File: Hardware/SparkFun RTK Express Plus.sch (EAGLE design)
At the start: 111 parts, among them J13 Internal, J16 MICRO-SD-PUSH-PUSH-EXT-PIN, J17 Qwiic Right Angle, J3 USB Female Type C Connector, J4 External, J5 USB Female Type C Connector, Q1 SIL2308-TP, Q2 MBT3904DW1T1, U1 74HC4052D, U10 MCP73833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

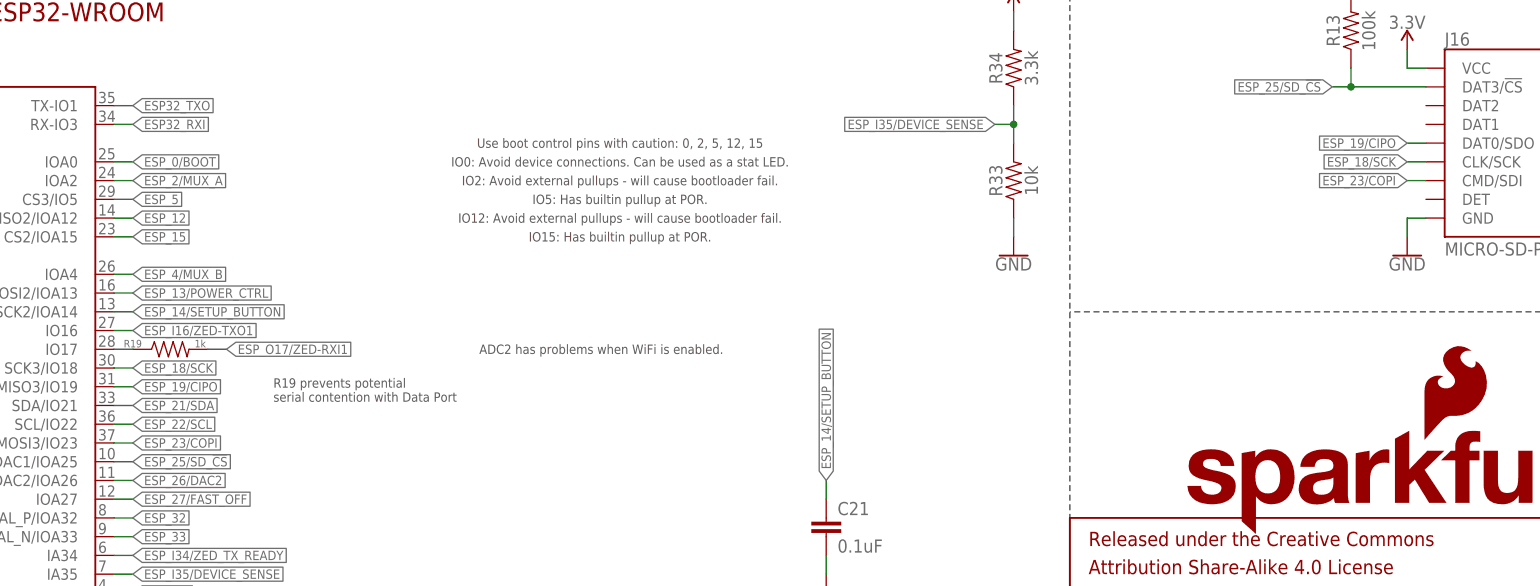
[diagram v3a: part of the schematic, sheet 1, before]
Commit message: v13 - Change to LIF overlay connector. Change ESP32 FP. Pull ground from accel.
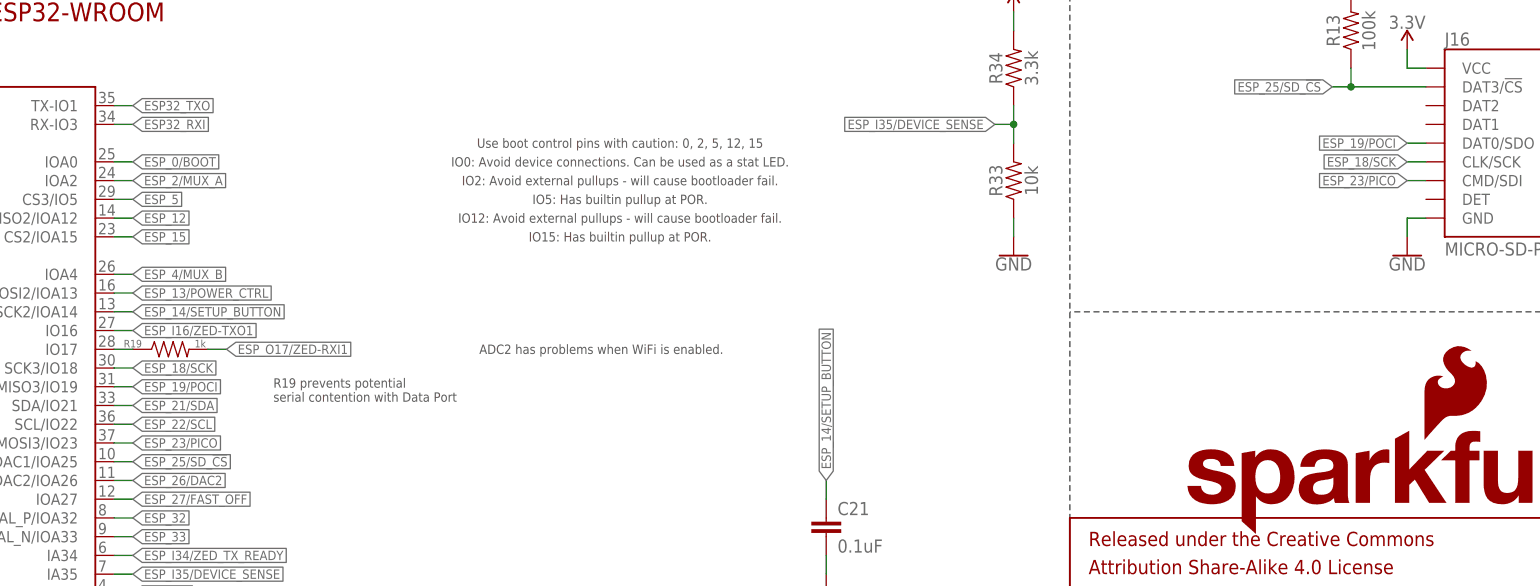
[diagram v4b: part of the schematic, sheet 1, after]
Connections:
- net ESP_19/CIPO renamed ESP_19/POCI
- net ESP_23/COPI renamed ESP_23/PICO
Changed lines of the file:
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@@
 <grid distance="0.1" unitdist="inch" unit="inch" style="lines" multiple="1" display="no" altdistance="0.01" altunitdist="inch" altunit="inch"/>
 <layers>
-<layer number="1" name="Top" color="4" fill="1" visible="yes" active="no"/>
-<layer number="2" name="Route2" color="1" fill="3" visible="yes" active="no"/>
-<layer number="3" name="Route3" color="4" fill="3" visible="yes" active="no"/>
-<layer number="4" name="Route4" color="1" fill="4" visible="yes" active="no"/>
-<layer number="5" name="Route5" color="4" fill="4" visible="yes" active="no"/>
-<layer number="6" name="Route6" color="1" fill="8" visible="yes" active="no"/>
-<layer number="7" name="Route7" color="4" fill="8" visible="yes" active="no"/>
-<layer number="8" name="Route8" color="1" fill="2" visible="yes" active="no"/>
-<layer number="9" name="Route9" color="4" fill="2" visible="yes" active="no"/>
-<layer number="10" name="Route10" color="1" fill="7" visible="yes" active="no"/>
-<layer number="11" name="Route11" color="4" fill="7" visible="yes" active="no"/>
-<layer number="12" name="Route12" color="1" fill="5" visible="yes" active="no"/>
-<layer number="13" name="Route13" color="4" fill="5" visible="yes" active="no"/>
-<layer number="14" name="Route14" color="1" fill="6" visible="yes" active="no"/>
-<layer number="15" name="Route15" color="4" fill="6" visible="yes" active="no"/>
-<layer number="16" name="Bottom" color="1" fill="1" visible="yes" active="no"/>
-<layer number="17" name="Pads" color="2" fill="1" visible="yes" active="no"/>
-<layer number="18" name="Vias" color="2" fill="1" visible="yes" active="no"/>
-<layer number="19" name="Unrouted" color="6" fill="1" visible="yes" active="no"/>
-<layer number="20" name="Dimension" color="24" fill="1" visible="yes" active="no"/>
-<layer number="21" name="tPlace" color="16" fill="1" visible="yes" active="no"/>
-<layer number="22" name="bPlace" color="14" fill="1" visible="yes" active="no"/>
-<layer number="23" name="tOrigins" color="15" fill="1" visible="yes" active="no"/>
-<layer number="24" name="bOrigins" color="15" fill="1" visible="yes" active="no"/>
-<layer number="25" name="tNames" color="7" fill="1" visible="yes" active="no"/>
-<layer number="26" name="bNames" color="7" fill="1" visible="yes" active="no"/>
-<layer number="27" name="tValues" color="7" fill="1" visible="yes" active="no"/>
-<layer number="28" name="bValues" color="7" fill="1" visible="yes" active="no"/>
+<layer number="1" name="Top" color="4" fill="1" visible="no" active="no"/>
+<layer number="2" name="Route2" color="1" fill="3" visible="no" active="no"/>
+<layer number="3" name="Route3" color="4" fill="3" visible="no" active="no"/>
+<layer number="4" name="Route4" color="1" fill="4" visible="no" active="no"/>
+<layer number="5" name="Route5" color="4" fill="4" visible="no" active="no"/>
+<layer number="6" name="Route6" color="1" fill="8" visible="no" active="no"/>
+<layer number="7" name="Route7" color="4" fill="8" visible="no" active="no"/>
+<layer number="8" name="Route8" color="1" fill="2" visible="no" active="no"/>
+<layer number="9" name="Route9" color="4" fill="2" visible="no" active="no"/>
+<layer number="10" name="Route10" color="1" fill="7" visible="no" active="no"/>
+<layer number="11" name="Route11" color="4" fill="7" visible="no" active="no"/>
+<layer number="12" name="Route12" color="1" fill="5" visible="no" active="no"/>
+<layer number="13" name="Route13" color="4" fill="5" visible="no" active="no"/>
+<layer number="14" name="Route14" color="1" fill="6" visible="no" active="no"/>
+<layer number="15" name="Route15" color="4" fill="6" visible="no" active="no"/>
+<layer number="16" name="Bottom" color="1" fill="1" visible="no" active="no"/>
+<layer number="17" name="Pads" color="2" fill="1" visible="no" active="no"/>
+<layer number="18" name="Vias" color="2" fill="1" visible="no" active="no"/>
+<layer number="19" name="Unrouted" color="6" fill="1" visible="no" active="no"/>
+<layer number="20" name="Dimension" color="24" fill="1" visible="no" active="no"/>
+<layer number="21" name="tPlace" color="16" fill="1" visible="no" active="no"/>
+<layer number="22" name="bPlace" color="14" fill="1" visible="no" active="no"/>
+<layer number="23" name="tOrigins" color="15" fill="1" visible="no" active="no"/>
+<layer number="24" name="bOrigins" color="15" fill="1" visible="no" active="no"/>
+<layer number="25" name="tNames" color="7" fill="1" visible="no" active="no"/>
+<layer number="26" name="bNames" color="7" fill="1" visible="no" active="no"/>
+<layer number="27" name="tValues" color="7" fill="1" visible="no" active="no"/>
+<layer number="28" name="bValues" color="7" fill="1" visible="no" active="no"/>
 <layer number="29" name="tStop" color="7" fill="3" visible="no" active="no"/>
 <layer number="30" name="bStop" color="7" fill="6" visible="no" active="no"/>
@@
 <layer number="35" name="tGlue" color="7" fill="4" visible="no" active="no"/>
 <layer number="36" name="bGlue" color="7" fill="5" visible="no" active="no"/>
-<layer number="37" name="tTest" color="7" fill="1" visible="yes" active="no"/>
-<layer number="38" name="bTest" color="7" fill="1" visible="yes" active="no"/>
+<layer number="37" name="tTest" color="7" fill="1" visible="no" active="no"/>
+<layer number="38" name="bTest" color="7" fill="1" visible="no" active="no"/>
 <layer number="39" name="tKeepout" color="4" fill="11" visible="no" active="no"/>
 <layer number="40" name="bKeepout" color="1" fill="11" visible="no" active="no"/>
@@
 <layer number="44" name="Drills" color="7" fill="1" visible="no" active="no"/>
 <layer number="45" name="Holes" color="7" fill="1" visible="no" active="no"/>
-<layer number="46" name="Milling" color="3" fill="1" visible="yes" active="no"/>
-<layer number="47" name="Measures" color="7" fill="1" visible="yes" active="no"/>
-<layer number="48" name="Document" color="7" fill="1" visible="yes" active="no"/>
-<layer number="49" name="Reference" color="7" fill="1" visible="yes" active="no"/>
-<layer number="50" name="dxf" color="7" fill="1" visible="yes" active="no"/>
-<layer number="51" name="tDocu" color="6" fill="1" visible="yes" active="no"/>
-<layer number="52" name="bDocu" color="7" fill="1" visible="yes" active="no"/>
-<layer number="53" name="tGND_GNDA" color="7" fill="9" visible="yes" active="no"/>
-<layer number="54" name="bGND_GNDA" color="1" fill="9" visible="yes" active="no"/>
-<layer number="56" name="wert" color="7" fill="1" visible="yes" active="no"/>
-<layer number="57" name="tCAD" color="7" fill="1" visible="yes" active="no"/>
-<layer number="58" name="bCAD" color="7" fill="1" visible="yes" active="no"/>
-<layer number="59" name="tCarbon" color="7" fill="1" visible="yes" active="no"/>
-<layer number="60" name="bCarbon" color="7" fill="1" visible="yes" active="no"/>
+<layer number="46" name="Milling" color="3" fill="1" visible="no" active="no"/>
+<layer number="47" name="Measures" color="7" fill="1" visible="no" active="no"/>
+<layer number="48" name="Document" color="7" fill="1" visible="no" active="no"/>
+<layer number="49" name="Reference" color="7" fill="1" visible="no" active="no"/>
+<layer number="50" name="dxf" color="7" fill="1" visible="no" active="no"/>
+<layer number="51" name="tDocu" color="6" fill="1" visible="no" active="no"/>
+<layer number="52" name="bDocu" color="7" fill="1" visible="no" active="no"/>
+<layer number="53" name="tGND_GNDA" color="7" fill="9" visible="no" active="no"/>
+<layer number="54" name="bGND_GNDA" color="1" fill="9" visible="no" active="no"/>
+<layer number="56" name="wert" color="7" fill="1" visible="no" active="no"/>
+<layer number="57" name="tCAD" color="7" fill="1" visible="no" active="no"/>
+<layer number="58" name="bCAD" color="7" fill="1" visible="no" active="no"/>
+<layer number="59" name="tCarbon" color="7" fill="1" visible="no" active="no"/>
+<layer number="60" name="bCarbon" color="7" fill="1" visible="no" active="no"/>
 <layer number="88" name="SimResults" color="9" fill="1" visible="yes" active="yes"/>
 <layer number="89" name="SimProbes" color="9" fill="1" visible="yes" active="yes"/>
@@
 </segment>
 </net>
-<net name="ESP_19/CIPO" class="0">
+<net name="ESP_19/POCI" class="0">
 <segment>
 <wire x1="200.66" y1="53.34" x2="203.2" y2="53.34" width="0.1524" layer="91"/>
@@
 </segment>
 </net>
-<net name="ESP_23/COPI" class="0">
+<net name="ESP_23/PICO" class="0">
 <segment>
 <wire x1="200.66" y1="45.72" x2="203.2" y2="45.72" width="0.1524" layer="91"/>

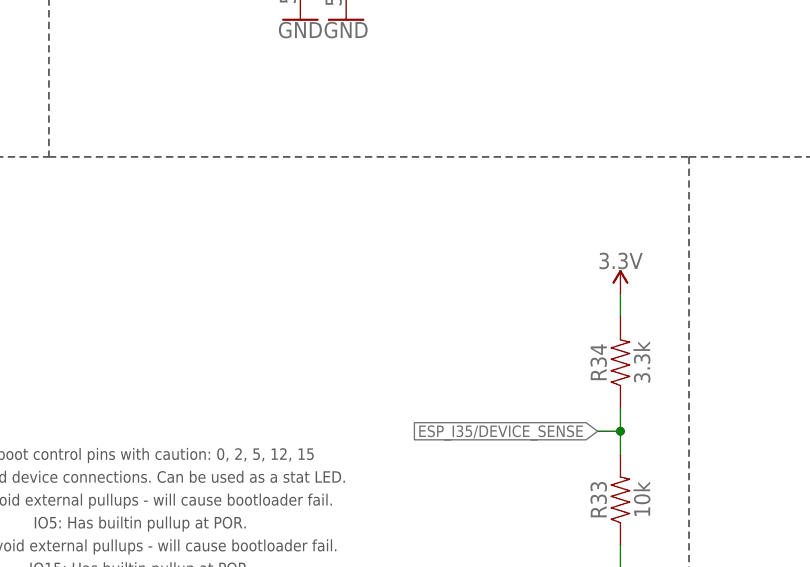
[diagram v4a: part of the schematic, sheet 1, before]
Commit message: Add ID Panel
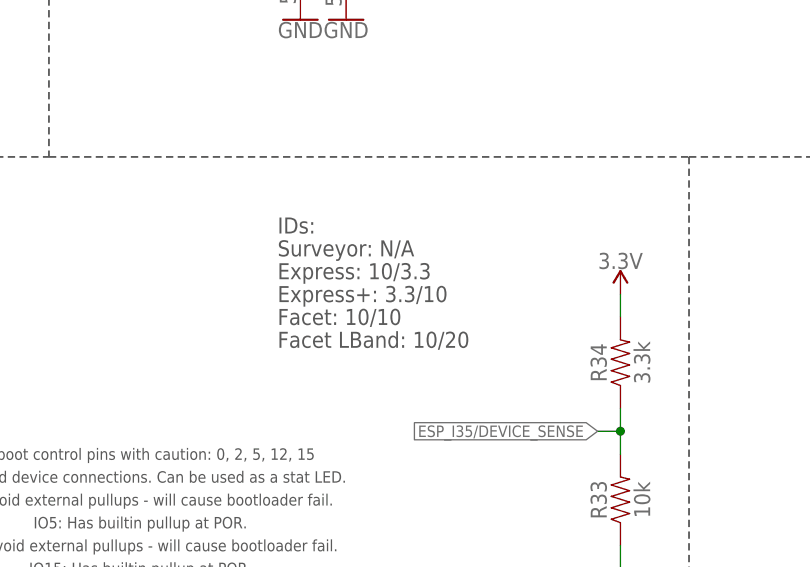
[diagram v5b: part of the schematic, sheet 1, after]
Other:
- note added: "Express+: 3.3/10"
- note added: "Express: 10/3.3"
- note added: "Facet LBand: 10/20"
- note added: "Facet: 10/10"
- note added: "IDs:"
- note added: "Surveyor: N/A"
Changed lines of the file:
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@@
 <wire x1="350.52" y1="198.12" x2="350.52" y2="279.4" width="0.2032" layer="97" style="longdash"/>
 <text x="58.42" y="68.58" size="1.27" layer="97" align="center">3.3V Signals Only</text>
+<text x="284.48" y="111.76" size="1.778" layer="97" align="center-left">IDs:</text>
+<text x="284.48" y="109.22" size="1.778" layer="97" align="center-left">Surveyor: N/A</text>
+<text x="284.48" y="106.68" size="1.778" layer="97" align="center-left">Express: 10/3.3</text>
+<text x="284.48" y="104.14" size="1.778" layer="97" align="center-left">Express+: 3.3/10</text>
+<text x="284.48" y="101.6" size="1.778" layer="97" align="center-left">Facet: 10/10</text>
+<text x="284.48" y="99.06" size="1.778" layer="97" align="center-left">Facet LBand: 10/20</text>
 </plain>
 <instances>
